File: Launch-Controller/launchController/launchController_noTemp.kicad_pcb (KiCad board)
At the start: 4 copper layers, 219.9 x 107.1 mm, 130 parts, among them J1 Relay Connector, J10 Relay Connector, J11 Raspberry_Pi_5, J12 Buck Connector, J13 26 pin Dsub, J14 DB25_Plug, J15 TVS Diode, J16 DB25_Plug, J17 DB25_Plug, J18 TVS Diode, J2 Relay Connector, J3 Relay Connector, J4 Relay Connector, J5 Relay Connector, J6 Relay Connector, J7 Relay Connector, J8 Relay Connector, J9 Relay Connector, Q1 NFET, Q10 NFET, Q2 NFET, Q3 NFET, Q4 NFET, Q5 NFET, Q6 NFET, Q7 NFET, Q8 NFET, Q9 NFET, U1 ADS1115, U2 ADS1115, U3 TCA9517ADGK

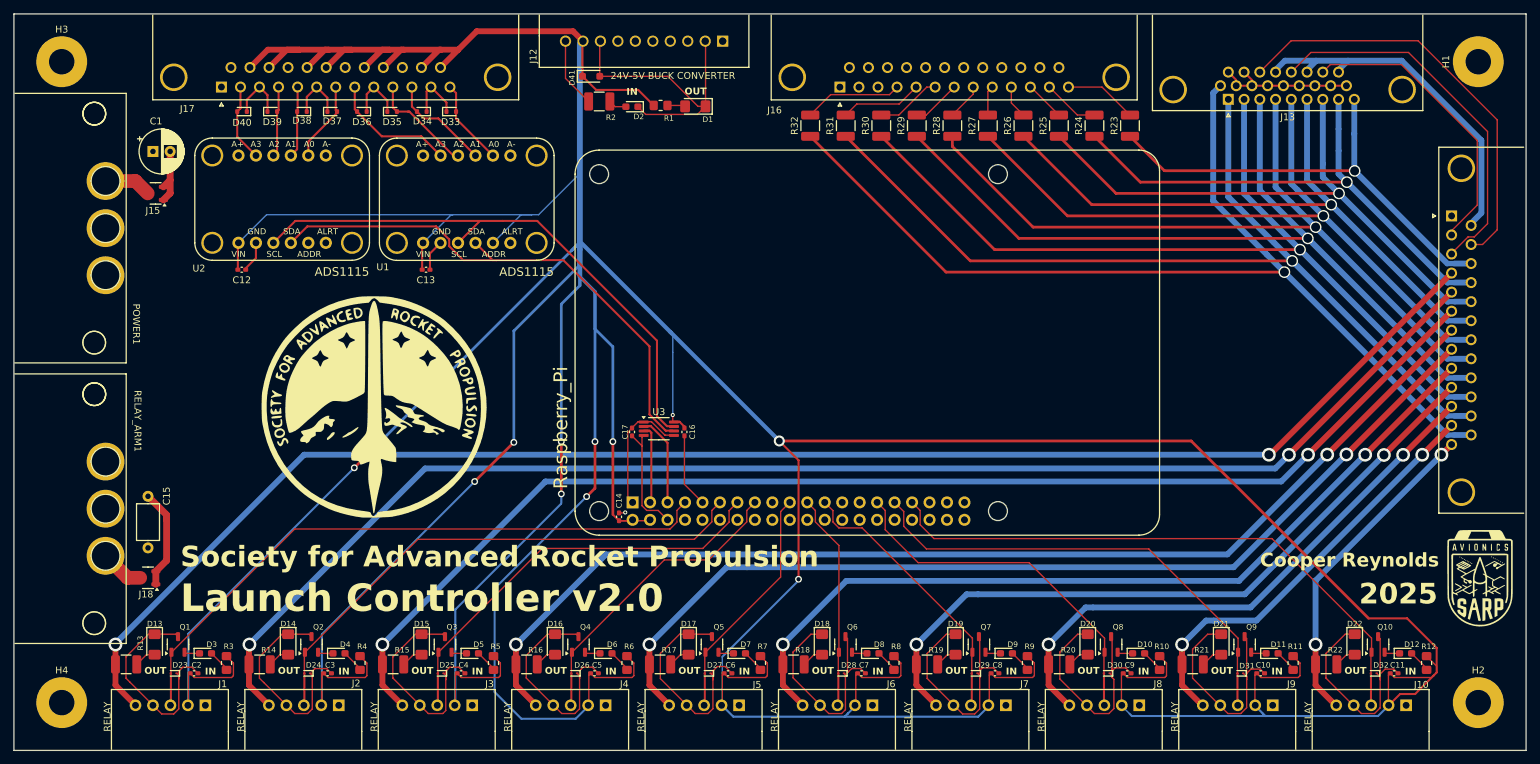
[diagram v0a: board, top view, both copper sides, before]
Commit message: via ground stitching main board
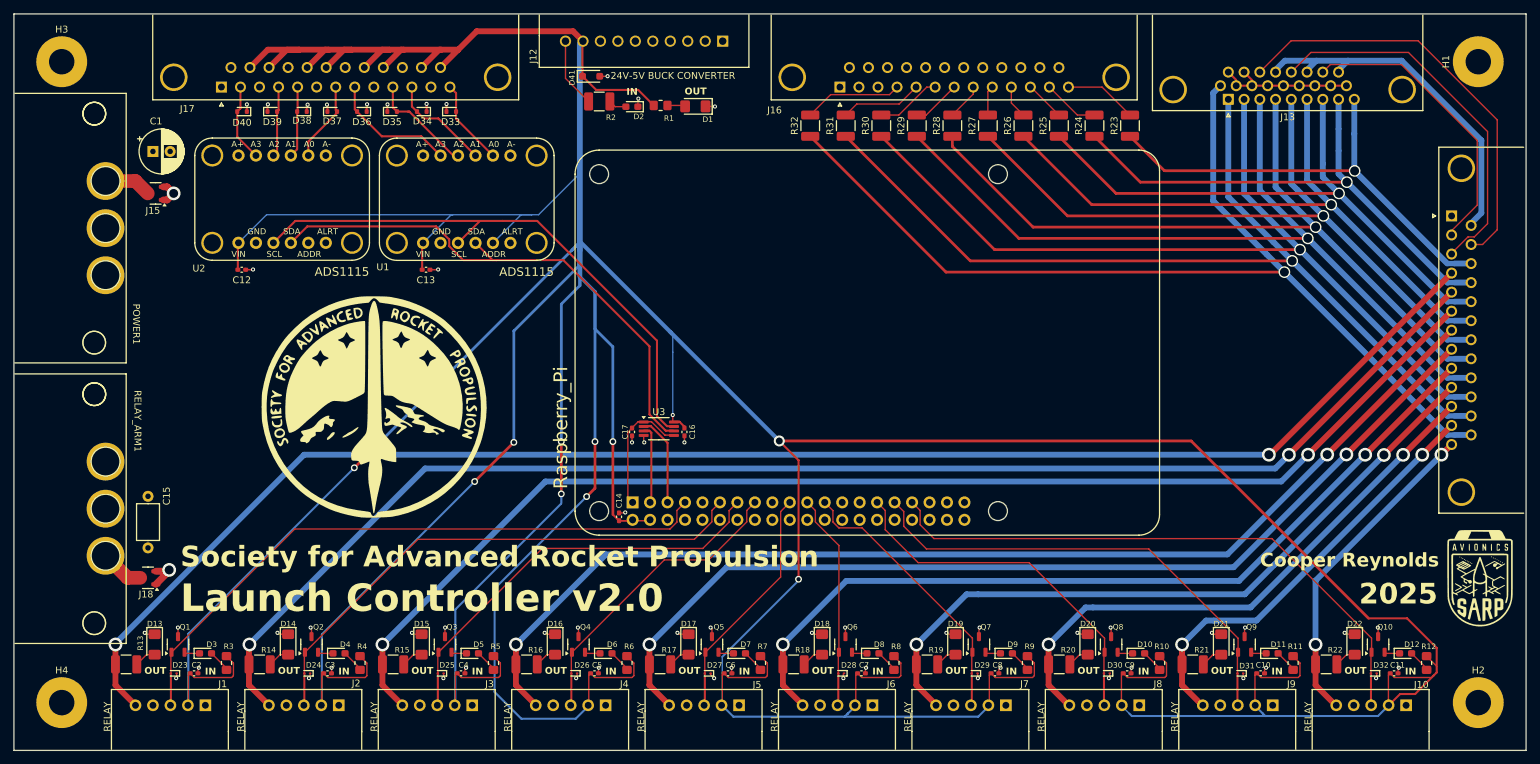
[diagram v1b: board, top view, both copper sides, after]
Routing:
- net GND: track 493.5 -> 94.2 mm, vias 1 -> 59
